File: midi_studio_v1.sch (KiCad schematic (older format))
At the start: 0 parts

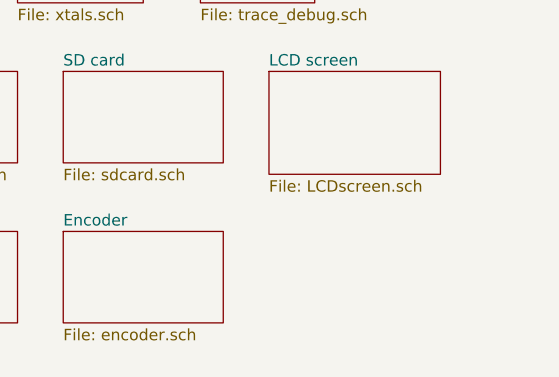
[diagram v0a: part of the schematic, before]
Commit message: First proposed pin layout of SODIMM connector
Will need to add GPIO / ADC pins as needed, but let's wait to see if we don't
need to use more pins.

Double-checked and fixed CODEC and MCU's power supply.
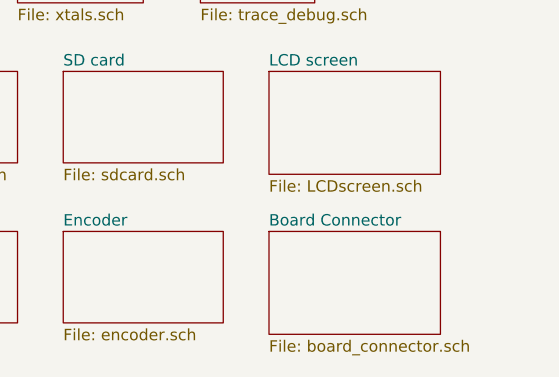
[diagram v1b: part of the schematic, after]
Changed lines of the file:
@@
 $Descr A4 11693 8268
 encoding utf-8
-Sheet 1 12
+Sheet 1 13
 Title "MIDI Studio Schematic"
 Date ""
@@
 F1 "encoder.sch" 50
 $EndSheet
+$Sheet
+S 3800 2200 750  450
+U 5D041201
+F0 "Board Connector" 50
+F1 "board_connector.sch" 50
+$EndSheet
 $EndSCHEMATC
